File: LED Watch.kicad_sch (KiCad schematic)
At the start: 142 parts, among them J1 AVR-ISP-6, J2 Lipo, J3 Coin Cell, SW1 SW_DPST, SW2 SW_DPST, U10 B39D3RGB-F6C0001HOU1930, U100 B39D3RGB-F6C0001HOU1930, U101 B39D3RGB-F6C0001HOU1930, U102 B39D3RGB-F6C0001HOU1930, U103 B39D3RGB-F6C0001HOU1930, U104 B39D3RGB-F6C0001HOU1930, U105 B39D3RGB-F6C0001HOU1930, U106 B39D3RGB-F6C0001HOU1930, U107 B39D3RGB-F6C0001HOU1930, U108 B39D3RGB-F6C0001HOU1930, U109 B39D3RGB-F6C0001HOU1930, U11 B39D3RGB-F6C0001HOU1930, U110 B39D3RGB-F6C0001HOU1930, U111 B39D3RGB-F6C0001HOU1930, U112 B39D3RGB-F6C0001HOU1930, U113 B39D3RGB-F6C0001HOU1930, U114 B39D3RGB-F6C0001HOU1930, U115 B39D3RGB-F6C0001HOU1930, U116 B39D3RGB-F6C0001HOU1930, U117 B39D3RGB-F6C0001HOU1930, U118 B39D3RGB-F6C0001HOU1930, U119 B39D3RGB-F6C0001HOU1930, U12 B39D3RGB-F6C0001HOU1930, U120 B39D3RGB-F6C0001HOU1930, U121 B39D3RGB-F6C0001HOU1930, U122 B39D3RGB-F6C0001HOU1930, U123 B39D3RGB-F6C0001HOU1930, U124 B39D3RGB-F6C0001HOU1930, U125 B39D3RGB-F6C0001HOU1930, U126 B39D3RGB-F6C0001HOU1930, U127 B39D3RGB-F6C0001HOU1930, U128 B39D3RGB-F6C0001HOU1930, U129 B39D3RGB-F6C0001HOU1930, U13 B39D3RGB-F6C0001HOU1930, U130 B39D3RGB-F6C0001HOU1930, U131 B39D3RGB-F6C0001HOU1930, U132 B39D3RGB-F6C0001HOU1930, U133 B39D3RGB-F6C0001HOU1930, U134 BMI160, U135 ATmega165PA-M, U14 B39D3RGB-F6C0001HOU1930, U15 B39D3RGB-F6C0001HOU1930, U16 B39D3RGB-F6C0001HOU1930, U17 B39D3RGB-F6C0001HOU1930, U18 B39D3RGB-F6C0001HOU1930, U19 B39D3RGB-F6C0001HOU1930, U2 B39D3RGB-F6C0001HOU1930, U20 B39D3RGB-F6C0001HOU1930, U21 B39D3RGB-F6C0001HOU1930, U22 B39D3RGB-F6C0001HOU1930, U23 B39D3RGB-F6C0001HOU1930, U24 B39D3RGB-F6C0001HOU1930, U25 B39D3RGB-F6C0001HOU1930, U26 B39D3RGB-F6C0001HOU1930, U27 B39D3RGB-F6C0001HOU1930, U28 B39D3RGB-F6C0001HOU1930, U29 B39D3RGB-F6C0001HOU1930, U3 B39D3RGB-F6C0001HOU1930, U30 B39D3RGB-F6C0001HOU1930, U31 B39D3RGB-F6C0001HOU1930, U32 B39D3RGB-F6C0001HOU1930, U33 B39D3RGB-F6C0001HOU1930, U34 B39D3RGB-F6C0001HOU1930, U35 B39D3RGB-F6C0001HOU1930, U36 B39D3RGB-F6C0001HOU1930, U37 B39D3RGB-F6C0001HOU1930, U38 B39D3RGB-F6C0001HOU1930, U39 B39D3RGB-F6C0001HOU1930, U4 B39D3RGB-F6C0001HOU1930, U40 B39D3RGB-F6C0001HOU1930, U41 B39D3RGB-F6C0001HOU1930, U42 B39D3RGB-F6C0001HOU1930, U43 B39D3RGB-F6C0001HOU1930, U44 B39D3RGB-F6C0001HOU1930, U45 B39D3RGB-F6C0001HOU1930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

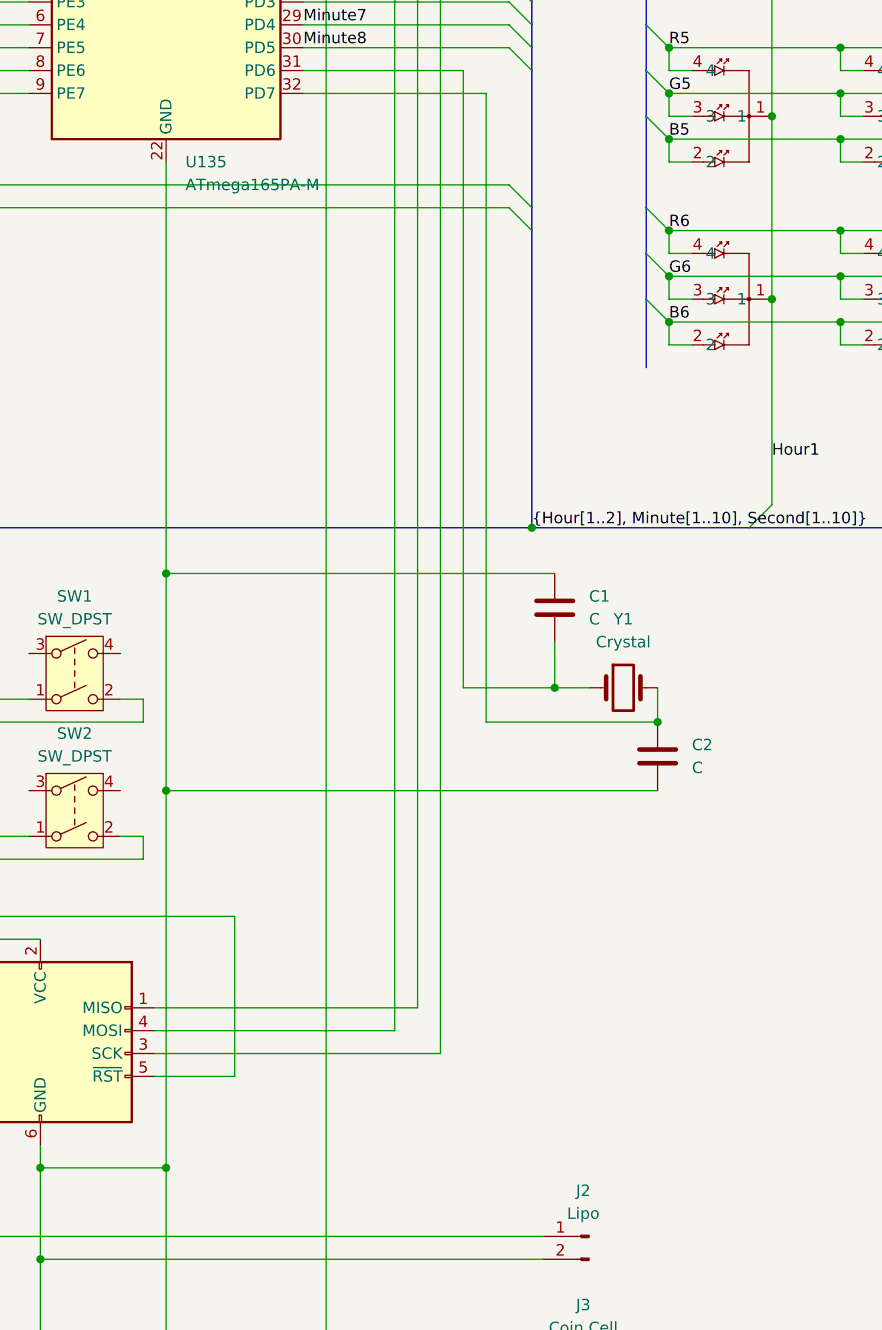
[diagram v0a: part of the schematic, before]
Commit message: traced out? iteration 1 at least.. passes an initial drc run.. I want to add a couple test regular white leds.. i should source and add for testing of potential single color board
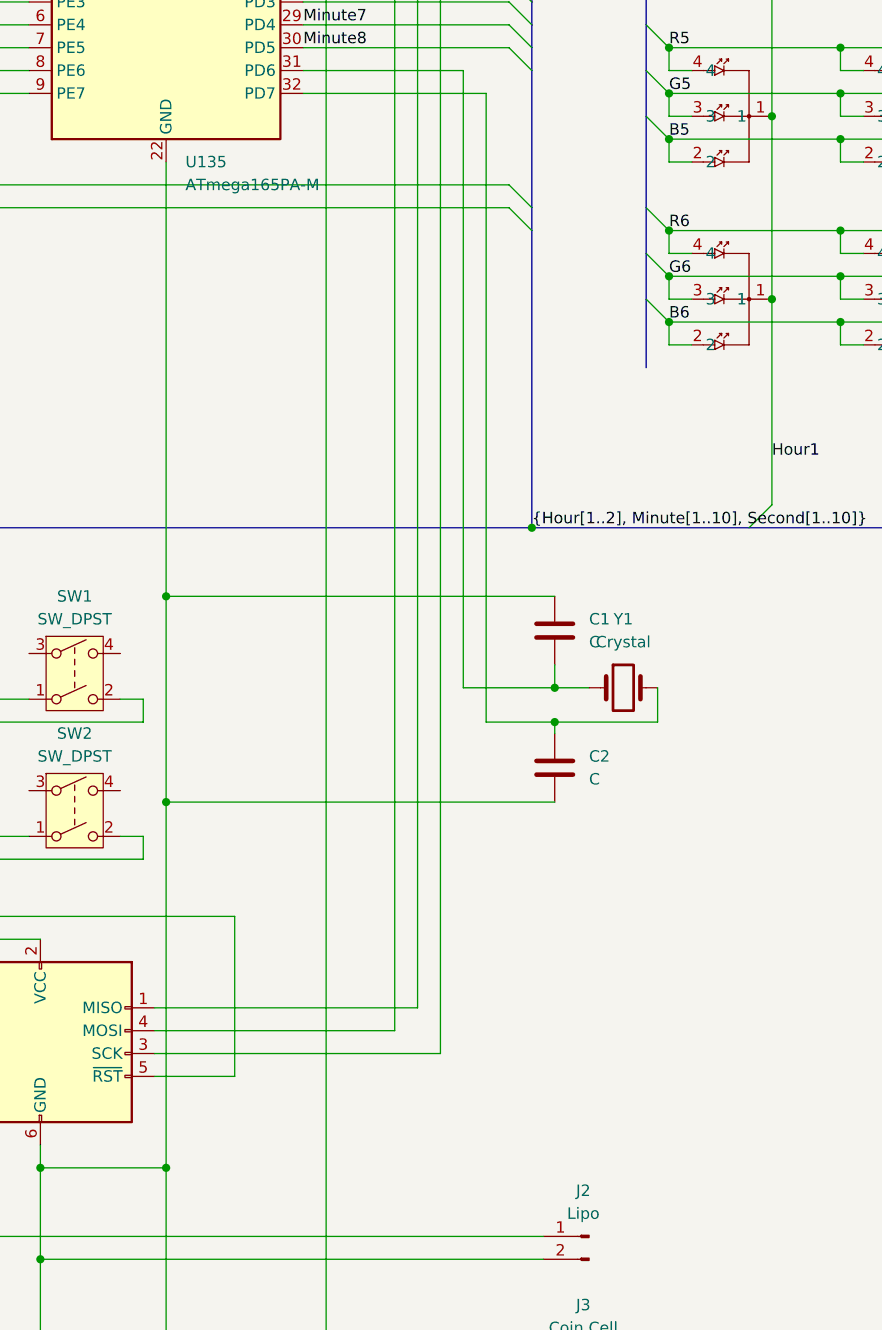
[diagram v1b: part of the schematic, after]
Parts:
- J1: footprint Connector_JST:JST_SH_BM06B-SRSS-TB_1x06-1MP_P1.00mm_Vertical -> Connector:Tag-Connect_TC2030-IDC-NL_2x03_P1.27mm_Vertical
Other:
- moved on the sheet: C1, C2
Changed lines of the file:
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@@
 	)
 	(junction
-		(at 119.38 196.85)
-		(diameter 0)
-		(color 0 0 0 0)
-	)
-	(junction
 		(at 342.9 106.68)
 		(diameter 0)
@@
 	)
 	(junction
+		(at 107.95 196.85)
+		(diameter 0)
+		(color 0 0 0 0)
+	)
+	(junction
 		(at 209.55 152.4)
 		(diameter 0)
@@
 	)
 	(junction
-		(at 64.77 204.47)
-		(diameter 0)
-		(color 0 0 0 0)
-	)
-	(junction
 		(at 139.7 66.04)
 		(diameter 0)
@@
 	)
 	(junction
+		(at 64.77 205.74)
+		(diameter 0)
+		(color 0 0 0 0)
+	)
+	(junction
 		(at 342.9 60.96)
 		(diameter 0)
@@
 	)
 	(junction
-		(at 64.77 180.34)
-		(diameter 0)
-		(color 0 0 0 0)
-	)
-	(junction
 		(at 374.65 86.36)
 		(diameter 0)
@@
 	)
 	(junction
+		(at 64.77 182.88)
+		(diameter 0)
+		(color 0 0 0 0)
+	)
+	(junction
 		(at 412.75 40.64)
 		(diameter 0)
@@
 	(wire
 		(pts
-			(xy 107.95 187.96) (xy 107.95 193.04)
+			(xy 107.95 190.5) (xy 107.95 193.04)
 		)
 		(stroke
@@
 	(wire
 		(pts
+			(xy 107.95 198.12) (xy 107.95 196.85)
+		)
+		(stroke
+			(width 0)
+			(type default)
+		)
+	)
+	(wire
+		(pts
 			(xy 488.95 86.36) (xy 508 86.36)
 		)
@@
 	(wire
 		(pts
+			(xy 107.95 196.85) (xy 119.38 196.85)
+		)
+		(stroke
+			(width 0)
+			(type default)
+		)
+	)
+	(wire
+		(pts
 			(xy 450.85 50.8) (xy 469.9 50.8)
 		)
@@
 	(wire
 		(pts
-			(xy 100.33 196.85) (xy 119.38 196.85)
+			(xy 100.33 196.85) (xy 107.95 196.85)
 		)
 		(stroke
@@
 	(wire
 		(pts
-			(xy 119.38 204.47) (xy 64.77 204.47)
+			(xy 107.95 205.74) (xy 64.77 205.74)
 		)
 		(stroke
@@
 	(wire
 		(pts
-			(xy 64.77 204.47) (xy 64.77 246.38)
+			(xy 64.77 134.62) (xy 64.77 182.88)
 		)
 		(stroke
@@
 	(wire
 		(pts
-			(xy 64.77 134.62) (xy 64.77 180.34)
-		)
-		(stroke
-			(width 0)
-			(type default)
-		)
-	)
-	(wire
-		(pts
 			(xy 171.45 43.18) (xy 171.45 40.64)
 		)
@@
 	(wire
 		(pts
-			(xy 107.95 180.34) (xy 64.77 180.34)
+			(xy 107.95 182.88) (xy 64.77 182.88)
 		)
 		(stroke
@@
 	(wire
 		(pts
-			(xy 64.77 180.34) (xy 64.77 204.47)
-		)
-		(stroke
-			(width 0)
-			(type default)
-		)
-	)
-	(wire
-		(pts
 			(xy 469.9 40.64) (xy 488.95 40.64)
 		)
@@
 	(wire
 		(pts
+			(xy 64.77 205.74) (xy 64.77 246.38)
+		)
+		(stroke
+			(width 0)
+			(type default)
+		)
+	)
+	(wire
+		(pts
 			(xy 527.05 106.68) (xy 527.05 109.22)
 		)
@@
 	(wire
 		(pts
+			(xy 64.77 182.88) (xy 64.77 205.74)
+		)
+		(stroke
+			(width 0)
+			(type default)
+		)
+	)
+	(wire
+		(pts
 			(xy 374.65 132.08) (xy 393.7 132.08)
 		)
@@
 			)
 		)
-		(property "Footprint" "Connector_JST:JST_SH_BM06B-SRSS-TB_1x06-1MP_P1.00mm_Vertical"
+		(property "Footprint" "Connector:Tag-Connect_TC2030-IDC-NL_2x03_P1.27mm_Vertical"
 			(at 46.99 232.41 90)
 			(effects
@@
 	(symbol
 		(lib_id "Device:C")
-		(at 119.38 200.66 0)
+		(at 107.95 201.93 0)
 		(unit 1)
 		(exclude_from_sim no)
@@
 		(fields_autoplaced yes)
 		(property "Reference" "C2"
-			(at 123.19 199.3899 0)
+			(at 111.76 200.6599 0)
 			(effects
 				(font
@@
 		)
 		(property "Value" "C"
-			(at 123.19 201.9299 0)
+			(at 111.76 203.1999 0)
 			(effects
 				(font
@@
 		)
 		(property "Footprint" "Capacitor_SMD:C_0201_0603Metric"
-			(at 120.3452 204.47 0)
+			(at 108.9152 205.74 0)
 			(effects
 				(font
@@
 		)
 		(property "Datasheet" "~"
-			(at 119.38 200.66 0)
+			(at 107.95 201.93 0)
 			(effects
 				(font
@@
 		)
 		(property "Description" "Unpolarized capacitor"
-			(at 119.38 200.66 0)
+			(at 107.95 201.93 0)
 			(effects
 				(font
@@
 	(symbol
 		(lib_id "Device:C")
-		(at 107.95 184.15 0)
+		(at 107.95 186.69 0)
 		(unit 1)
 		(exclude_from_sim no)
@@
 		(fields_autoplaced yes)
 		(property "Reference" "C1"
-			(at 111.76 182.8799 0)
+			(at 111.76 185.4199 0)
 			(effects
 				(font
@@
 		)
 		(property "Value" "C"
-			(at 111.76 185.4199 0)
+			(at 111.76 187.9599 0)
 			(effects
 				(font
@@
 		)
 		(property "Footprint" "Capacitor_SMD:C_0201_0603Metric"
-			(at 108.9152 187.96 0)
+			(at 108.9152 190.5 0)
 			(effects
 				(font
@@
 		)
 		(property "Datasheet" "~"
-			(at 107.95 184.15 0)
+			(at 107.95 186.69 0)
 			(effects
 				(font
@@
 		)
 		(property "Description" "Unpolarized capacitor"
-			(at 107.95 184.15 0)
+			(at 107.95 186.69 0)
 			(effects
 				(font

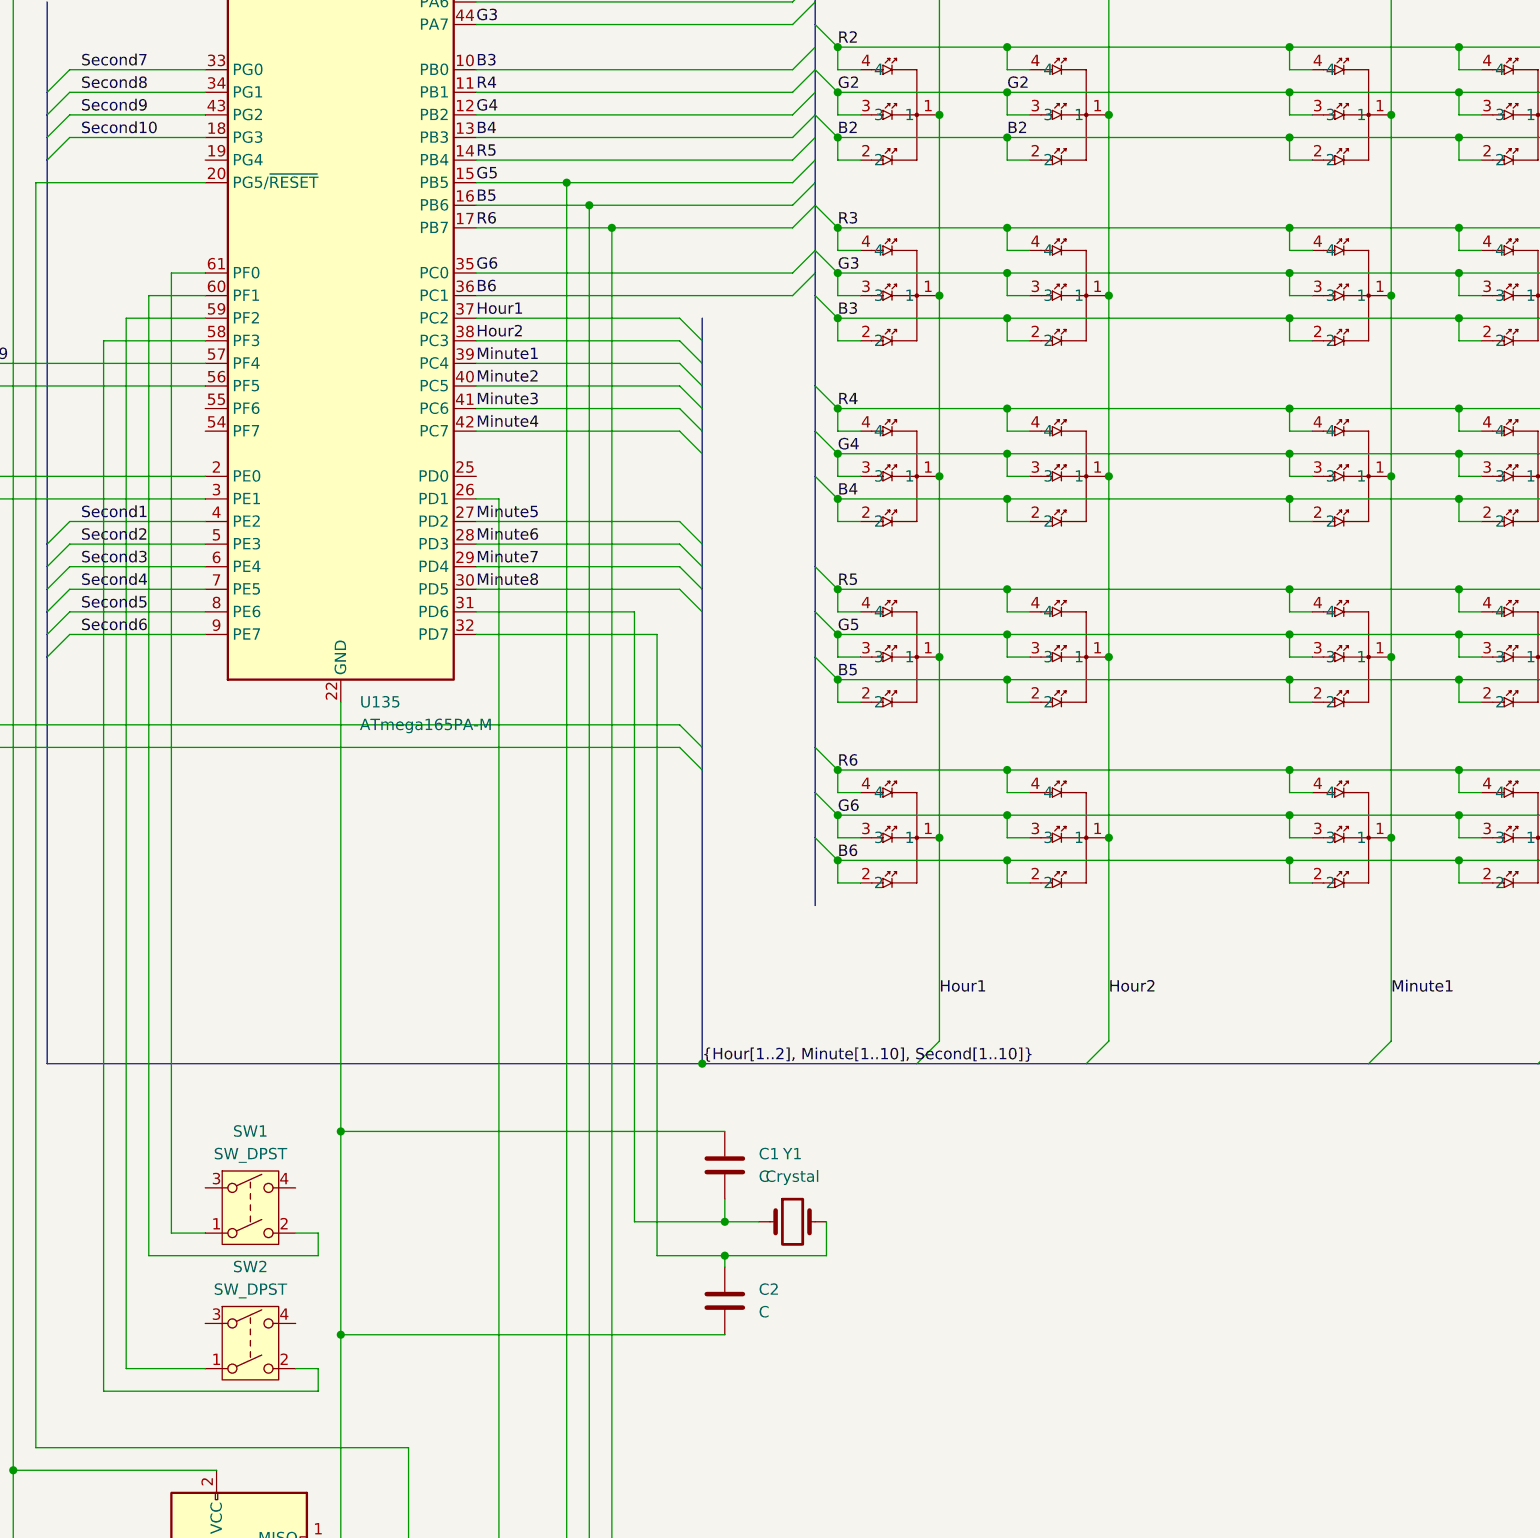
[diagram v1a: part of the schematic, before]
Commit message: pulled vias from under chip and added 4 0603 pads for testing options
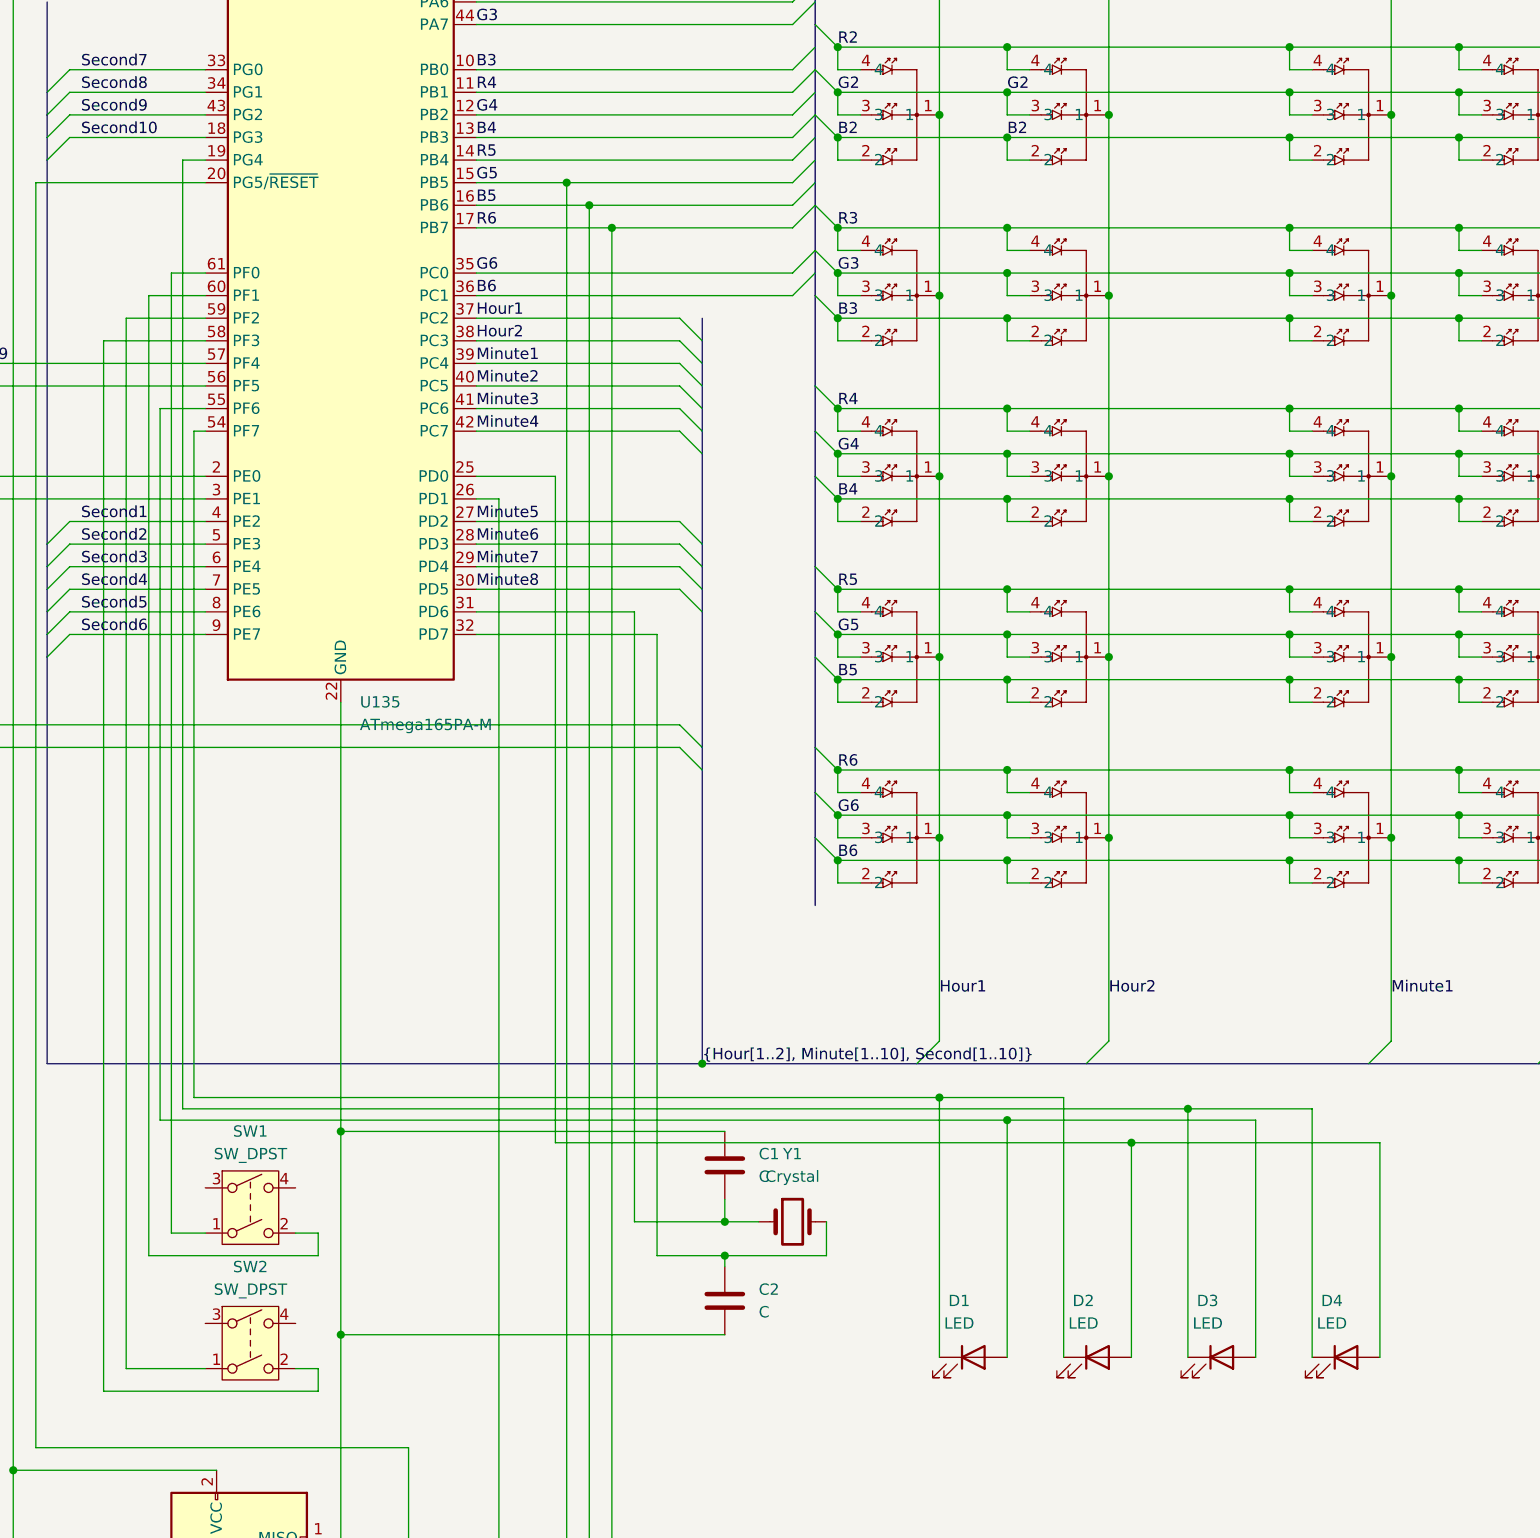
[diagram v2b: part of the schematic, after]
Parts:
- added D1, D2, D3, D4: LED, LED_SMD:LED_0201_0603Metric, symbol Device:LED
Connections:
- net at U135.19 (PG4): now also D3.1 (K), D4.1 (K)
- net at U135.25 (PD0): now also D2.2 (A), D4.2 (A)
- net at U135.54 (PF7): now also D1.1 (K), D2.1 (K)
- net at U135.55 (PF6): now also D1.2 (A), D3.2 (A)
